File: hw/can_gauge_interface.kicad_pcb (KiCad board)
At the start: 4 copper layers, 75 x 75 mm, 61 parts, among them J1 Conn_02x04_Top_Bottom, J2 Analog, J3 Power debug, J4 Power debug, J5 SPI debug, J6 I^{2}C debug, J7 CAN debug, J8 SWD, U1 STM32C092CBT6, U2 TPS5430DDA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

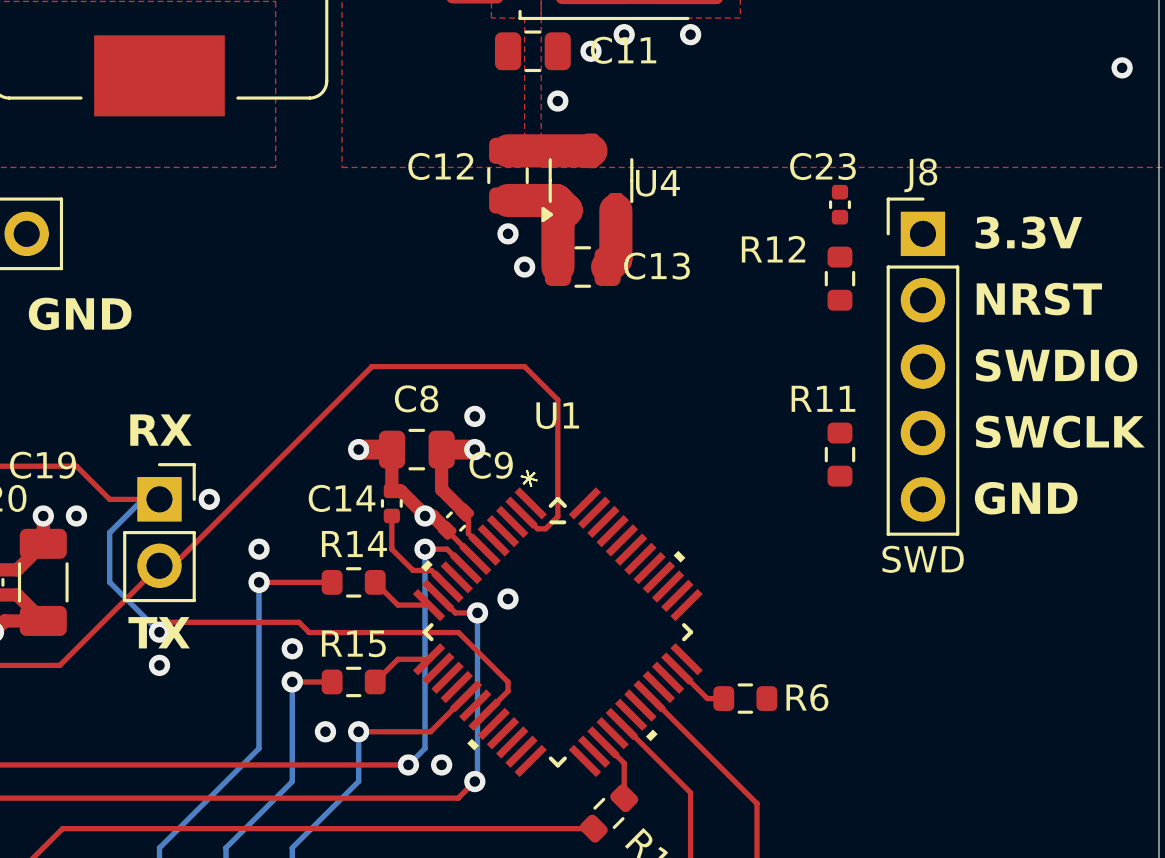
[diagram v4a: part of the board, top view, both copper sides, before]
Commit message: pcb: swd routing
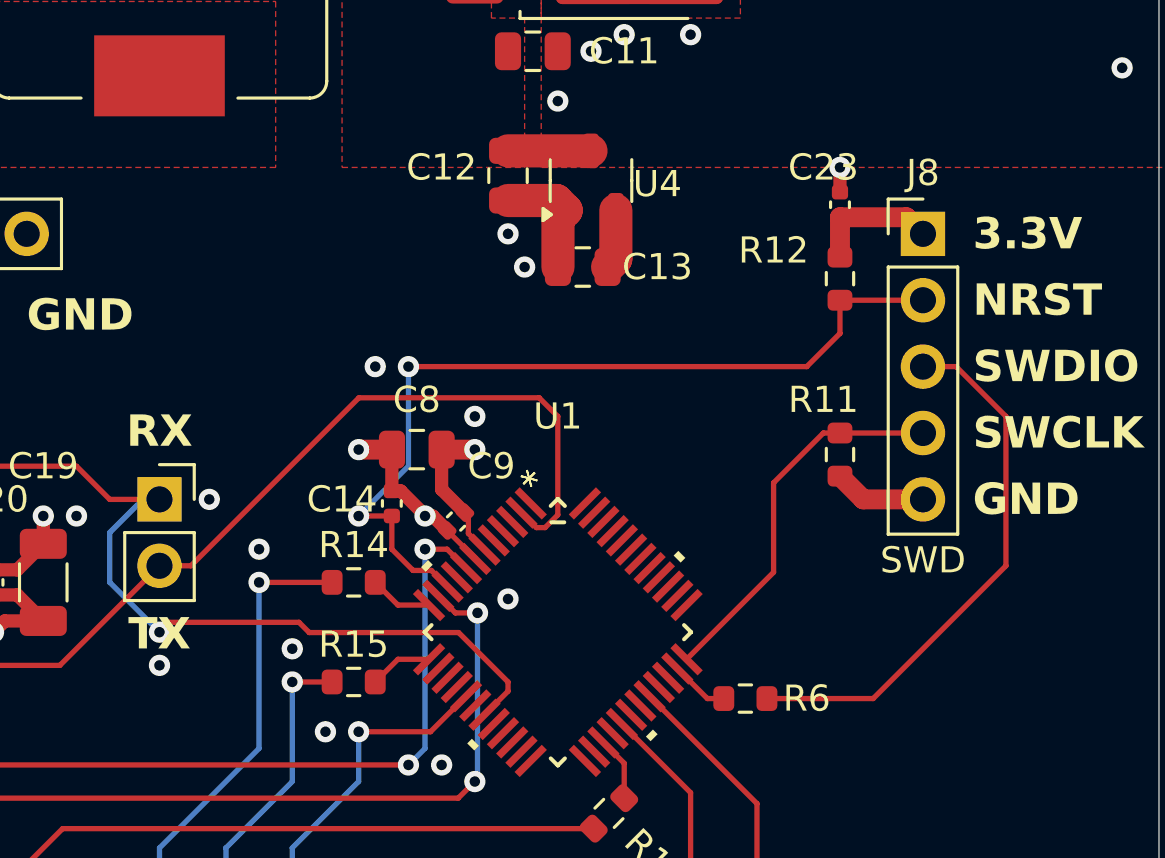
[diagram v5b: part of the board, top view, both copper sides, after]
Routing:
- net NRST: track 3.99 -> 33.2 mm, vias 0 -> 2
- net SWDIO: track 0.00 -> 20.9 mm
- net SWCLK: track 0.00 -> 14.6 mm
- net +3.3V: track 30.5 -> 35.5 mm
- net GND: track 55.6 -> 60.1 mm, vias 51 -> 53
- net CAN_TX: track 35.4 -> 33.9 mm
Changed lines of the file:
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@@
+	)
+	(segment
+		(start 140.97 81.28)
+		(end 138.685 81.28)
+		(width 0.762)
+		(layer "F.Cu")
+		(net 1)
 	)
 	(segment
@@
 	)
 	(segment
+		(start 138.685 81.28)
+		(end 137.795 80.39)
+		(width 0.762)
+		(layer "F.Cu")
+		(net 1)
+	)
+	(segment
 		(start 107.906178 108.541178)
 		(end 107.95 108.585)
@@
 		(start 103.7336 85.09)
 		(end 102.235 85.09)
+		(width 0.508)
+		(layer "F.Cu")
+		(net 1)
+	)
+	(segment
+		(start 137.795 69.525)
+		(end 137.795 68.58)
 		(width 0.508)
 		(layer "F.Cu")
@@
 	)
 	(via
+		(at 137.795 68.58)
+		(size 0.8128)
+		(drill 0.4)
+		(layers "F.Cu" "B.Cu")
+		(free yes)
+		(net 1)
+	)
+	(via
 		(at 132.08 55.245)
 		(size 0.8128)
@@
 	(via
 		(at 123.825 78.105)
+		(size 0.8128)
+		(drill 0.4)
+		(layers "F.Cu" "B.Cu")
+		(free yes)
+		(net 1)
+	)
+	(via
+		(at 120.015 76.2)
 		(size 0.8128)
 		(drill 0.4)
@@
 	)
 	(segment
+		(start 140.335 70.485)
+		(end 140.97 71.12)
+		(width 0.762)
+		(layer "F.Cu")
+		(net 7)
+	)
+	(segment
 		(start 103.505 104.14)
 		(end 103.505 102.235)
@@
 		(end 137.16 102.235)
 		(width 0.508)
+		(layer "F.Cu")
+		(net 7)
+	)
+	(segment
+		(start 137.795 70.485)
+		(end 140.335 70.485)
+		(width 0.762)
 		(layer "F.Cu")
 		(net 7)
@@
 	)
 	(segment
+		(start 137.795 70.485)
+		(end 137.795 72.01)
+		(width 0.762)
+		(layer "F.Cu")
+		(net 7)
+	)
+	(segment
 		(start 131.445 104.775)
 		(end 130.81 104.775)
@@
 	)
 	(segment
+		(start 136.525 76.2)
+		(end 137.795 74.93)
+		(width 0.2032)
+		(layer "F.Cu")
+		(net 9)
+	)
+	(segment
+		(start 120.65 81.915)
+		(end 119.38 81.915)
+		(width 0.2032)
+		(layer "F.Cu")
+		(net 9)
+	)
+	(segment
+		(start 137.795 74.93)
+		(end 137.795 73.66)
+		(width 0.2032)
+		(layer "F.Cu")
+		(net 9)
+	)
+	(segment
 		(start 122.781119 84.615991)
 		(end 122.163236 83.998108)
@@
 	)
 	(segment
+		(start 140.97 73.66)
+		(end 137.795 73.66)
+		(width 0.2032)
+		(layer "F.Cu")
+		(net 9)
+	)
+	(segment
+		(start 121.285 76.2)
+		(end 136.525 76.2)
+		(width 0.2032)
+		(layer "F.Cu")
+		(net 9)
+	)
+	(segment
 		(start 121.463108 83.998108)
 		(end 120.65 83.185)
@@
 		(net 9)
 	)
+	(via
+		(at 121.285 76.2)
+		(size 0.8128)
+		(drill 0.4)
+		(layers "F.Cu" "B.Cu")
+		(net 9)
+	)
+	(via
+		(at 119.38 81.915)
+		(size 0.8128)
+		(drill 0.4)
+		(layers "F.Cu" "B.Cu")
+		(net 9)
+	)
+	(segment
+		(start 119.38 81.915)
+		(end 121.285 80.01)
+		(width 0.2032)
+		(layer "B.Cu")
+		(net 9)
+	)
+	(segment
+		(start 121.285 80.01)
+		(end 121.285 76.2)
+		(width 0.2032)
+		(layer "B.Cu")
+		(net 9)
+	)
 	(segment
 		(start 122.764338 83.185)
@@
 	)
 	(segment
+		(start 126.511839 82.359449)
+		(end 127 81.871288)
+		(width 0.2032)
+		(layer "F.Cu")
+		(net 34)
+	)
+	(segment
+		(start 127 81.871288)
+		(end 127 78.105)
+		(width 0.2032)
+		(layer "F.Cu")
+		(net 34)
+	)
+	(segment
 		(start 111.76 83.82)
 		(end 107.95 87.63)
@@
 	)
 	(segment
-		(start 127 81.936342)
-		(end 127 77.47)
-		(width 0.2032)
-		(layer "F.Cu")
-		(net 34)
-	)
-	(segment
 		(start 107.95 87.63)
 		(end 105.0036 87.63)
@@
 	)
 	(segment
-		(start 127 77.47)
-		(end 125.73 76.2)
+		(start 127 78.105)
+		(end 126.2878 77.3928)
 		(width 0.2032)
 		(layer "F.Cu")
@@
 	)
 	(segment
-		(start 125.73 76.2)
-		(end 119.889099 76.2)
+		(start 112.962081 83.82)
+		(end 111.76 83.82)
 		(width 0.2032)
 		(layer "F.Cu")
@@
 	)
 	(segment
-		(start 126.530893 82.405449)
-		(end 127 81.936342)
+		(start 126.2878 77.3928)
+		(end 119.389281 77.3928)
 		(width 0.2032)
 		(layer "F.Cu")
@@
 	)
 	(segment
+		(start 126.181431 82.359449)
+		(end 126.511839 82.359449)
+		(width 0.2032)
+		(layer "F.Cu")
+		(net 34)
+	)
+	(segment
+		(start 119.389281 77.3928)
+		(end 112.962081 83.82)
+		(width 0.2032)
+		(layer "F.Cu")
+		(net 34)
+	)
+	(segment
 		(start 125.609546 81.787564)
-		(end 126.227431 82.405449)
+		(end 126.181431 82.359449)
 		(width 0.2032)
 		(layer "F.Cu")
@@
 	)
 	(segment
-		(start 112.269099 83.82)
-		(end 111.76 83.82)
-		(width 0.2032)
-		(layer "F.Cu")
-		(net 34)
-	)
-	(segment
-		(start 126.227431 82.405449)
-		(end 126.530893 82.405449)
-		(width 0.2032)
-		(layer "F.Cu")
-		(net 34)
-	)
-	(segment
-		(start 119.889099 76.2)
-		(end 112.269099 83.82)
-		(width 0.2032)
-		(layer "F.Cu")
-		(net 34)
-	)
-	(segment
+		(start 144.145 83.82)
+		(end 144.145 78.105)
+		(width 0.2032)
+		(layer "F.Cu")
+		(net 35)
+	)
+	(segment
+		(start 144.145 78.105)
+		(end 142.24 76.2)
+		(width 0.2032)
+		(layer "F.Cu")
+		(net 35)
+	)
+	(segment
+		(start 142.24 76.2)
+		(end 140.97 76.2)
+		(width 0.2032)
+		(layer "F.Cu")
+		(net 35)
+	)
+	(segment
+		(start 139.065 88.9)
+		(end 144.145 83.82)
+		(width 0.2032)
+		(layer "F.Cu")
+		(net 35)
+	)
+	(segment
+		(start 135 88.9)
+		(end 139.065 88.9)
+		(width 0.2032)
+		(layer "F.Cu")
+		(net 35)
+	)
+	(segment
+		(start 137.795 78.74)
+		(end 140.97 78.74)
+		(width 0.2032)
+		(layer "F.Cu")
+		(net 38)
+	)
+	(segment
+		(start 135.255 84.06789)
+		(end 135.255 80.645)
+		(width 0.2032)
+		(layer "F.Cu")
+		(net 38)
+	)
+	(segment
+		(start 131.925989 87.396901)
+		(end 135.255 84.06789)
+		(width 0.2032)
+		(layer "F.Cu")
+		(net 38)
+	)
+	(segment
+		(start 137.16 78.74)
+		(end 137.795 78.74)
+		(width 0.2032)
+		(layer "F.Cu")
+		(net 38)
+	)
+	(segment
+		(start 135.255 80.645)
+		(end 137.16 78.74)
+		(width 0.2032)
+		(layer "F.Cu")
+		(net 38)
+	)
+	(segment

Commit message: pcb: 3v3 routing
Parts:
- moved R12 3.59 mm to (135.3, 75.4)
- moved R9 1.91 mm to (102.2, 102.2)
- moved C15 1.62 mm to (106.0, 101.9), turned to -90 degrees
- moved C23 1.33 mm to (138.4, 68.8)
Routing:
- net +3.3V: track 35.5 -> 136.2 mm, vias 3 -> 6
- net GND: track 60.1 -> 65.6 mm, vias 53 -> 55
- net DAC_~{CS}: track 34.7 -> 35.5 mm
- net NRST: track 33.2 -> 32.5 mm
- added copper zone on F.Cu, net +3.3V

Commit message: pcb: 5v routing
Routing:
- net +5V: track 8.30 -> 74.9 mm, vias 1 -> 4
- net GND: vias 55 -> 59
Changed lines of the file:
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@@
+	)
+	(via
+		(at 108.585 81.915)
+		(size 0.8128)
+		(drill 0.4)
+		(layers "F.Cu" "B.Cu")
+		(free yes)
+		(net 1)
 	)
 	(via
@@
 	)
 	(via
-		(at 108.585 81.915)
-		(size 0.8128)
-		(drill 0.4)
-		(layers "F.Cu" "B.Cu")
-		(free yes)
-		(net 1)
-	)
-	(via
 		(at 121.92 81.915)
 		(size 0.8128)
@@
 	)
 	(via
+		(at 113.03 109.855)
+		(size 0.8128)
+		(drill 0.4)
+		(layers "F.Cu" "B.Cu")
+		(free yes)
+		(net 1)
+	)
+	(via
 		(at 125.095 85.09)
 		(size 0.8128)
@@
 	)
 	(via
+		(at 119.38 68.58)
+		(size 0.8128)
+		(drill 0.4)
+		(layers "F.Cu" "B.Cu")
+		(free yes)
+		(net 1)
+	)
+	(via
 		(at 148.59 64.77)
 		(size 0.8128)
@@
 	)
 	(via
+		(at 100.329999 73.025)
+		(size 0.8128)
+		(drill 0.4)
+		(layers "F.Cu" "B.Cu")
+		(free yes)
+		(net 1)
+	)
+	(via
 		(at 122.555 91.44)
 		(size 0.8128)
@@
 	(via
 		(at 90.17 60.96)
+		(size 0.8128)
+		(drill 0.4)
+		(layers "F.Cu" "B.Cu")
+		(free yes)
+		(net 1)
+	)
+	(via
+		(at 108.585 78.105)
 		(size 0.8128)
 		(drill 0.4)
@@
 	)
 	(segment
+		(start 111.125 110.49)
+		(end 111.76 109.855)
+		(width 0.762)
+		(layer "F.Cu")
+		(net 5)
+	)
+	(segment
 		(start 105.41 83.975)
 		(end 103.8886 83.975)
@@
 	)
 	(segment
-		(start 107.315 82.98)
-		(end 107.315 81.915)
-		(width 0.508)
+		(start 101.599999 71.12)
+		(end 101.6 72.39)
+		(width 1.27)
 		(layer "F.Cu")
 		(net 5)
@@
 	)
 	(segment
+		(start 101.6 72.39)
+		(end 107.315 78.105)
+		(width 1.27)
+		(layer "F.Cu")
+		(net 5)
+	)
+	(segment
 		(start 106.32 83.975)
 		(end 107.315 82.98)
@@
 	)
 	(segment
+		(start 111.125 111.76)
+		(end 111.125 110.49)
+		(width 0.762)
+		(layer "F.Cu")
+		(net 5)
+	)
+	(segment
 		(start 105.41 83.975)
 		(end 106.32 83.975)
@@
 	)
 	(segment
+		(start 107.315 81.915)
+		(end 107.315 82.98)
+		(width 1.27)
+		(layer "F.Cu")
+		(net 5)
+	)
+	(segment
 		(start 103.8886 83.975)
 		(end 103.7336 83.82)
@@
 	(via
 		(at 107.315 81.915)
-		(size 0.8128)
-		(drill 0.4)
-		(layers "F.Cu" "B.Cu")
-		(net 5)
-	)
+		(size 1.2192)
+		(drill 0.7)
+		(layers "F.Cu" "B.Cu")
+		(net 5)
+	)
+	(via
+		(at 120.015 67.31)
+		(size 1.2192)
+		(drill 0.7)
+		(layers "F.Cu" "B.Cu")
+		(free yes)
+		(net 5)
+	)
+	(via
+		(at 107.315 78.105)
+		(size 1.2192)
+		(drill 0.7)
+		(layers "F.Cu" "B.Cu")
+		(net 5)
+	)
+	(via
+		(at 111.76 109.855)
+		(size 1.2192)
+		(drill 0.7)
+		(layers "F.Cu" "B.Cu")
+		(net 5)
+	)
+	(segment
+		(start 107.95 88.9)
+		(end 107.95 106.045)
+		(width 1.27)
+		(layer "B.Cu")
+		(net 5)
+	)
+	(segment
+		(start 120.015 67.31)
+		(end 102.87 67.31)
+		(width 1.27)
+		(layer "B.Cu")
+		(net 5)
+	)
+	(segment
+		(start 107.315 78.105)
+		(end 107.315 81.915)
+		(width 1.27)
+		(layer "B.Cu")
+		(net 5)
+	)
+	(segment
+		(start 101.599999 68.580001)
+		(end 101.599999 71.12)
+		(width 1.27)
+		(layer "B.Cu")
+		(net 5)
+	)
+	(segment
+		(start 107.95 106.045)
+		(end 111.76 109.855)
+		(width 1.27)
+		(layer "B.Cu")
+		(net 5)
+	)
+	(segment
+		(start 102.87 67.31)
+		(end 101.599999 68.580001)
+		(width 1.27)
+		(layer "B.Cu")
+		(net 5)
+	)
+	(segment
+		(start 107.315 88.265)
+		(end 107.95 88.9)
+		(width 1.27)
+		(layer "B.Cu")
+		(net 5)
+	)
+	(segment
+		(start 107.315 81.915)
+		(end 107.315 88.265)
+		(width 1.27)
+		(layer "B.Cu")
+		(net 5)
+	)

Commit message: pcb: drc
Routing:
- net GND: track 65.6 -> 69.3 mm, vias 59 -> 64
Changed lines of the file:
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@@
 			)
 		)
-		(pad "" smd roundrect
-			(at -0.5 -0.5 315)
-			(size 0.806226 0.806226)
-			(layers "F.Paste")
-			(roundrect_rratio 0.25)
-		)
-		(pad "" smd roundrect
-			(at -0.5 0.5 315)
-			(size 0.806226 0.806226)
-			(layers "F.Paste")
-			(roundrect_rratio 0.25)
-		)
 		(pad "" smd custom
 			(at -0.499999 -1.2875 315)
@@
 			)
 		)
-		(pad "" smd roundrect
-			(at 0.5 -0.5 315)
-			(size 0.806226 0.806226)
-			(layers "F.Paste")
-			(roundrect_rratio 0.25)
-		)
-		(pad "" smd roundrect
-			(at 0.5 0.5 315)
-			(size 0.806226 0.806226)
-			(layers "F.Paste")
-			(roundrect_rratio 0.25)
-		)
 		(pad "" smd custom
 			(at 1.2875 -1.2875 315)
@@
 			(pintype "power_in")
 		)
-		(pad "21" thru_hole circle
-			(at -1 -1 315)
-			(size 0.5 0.5)
-			(drill 0.2)
-			(property pad_prop_heatsink)
-			(layers "*.Cu")
-			(remove_unused_layers no)
-			(net 1 "GND")
-			(pinfunction "EP")
-			(pintype "passive")
-		)
-		(pad "21" thru_hole circle
-			(at -1 0 315)
-			(size 0.5 0.5)
-			(drill 0.2)
-			(property pad_prop_heatsink)
-			(layers "*.Cu")
-			(remove_unused_layers no)
-			(net 1 "GND")
-			(pinfunction "EP")
-			(pintype "passive")
-		)
-		(pad "21" thru_hole circle
-			(at -1 1 315)
-			(size 0.5 0.5)
-			(drill 0.2)
-			(property pad_prop_heatsink)
-			(layers "*.Cu")
-			(remove_unused_layers no)
-			(net 1 "GND")
-			(pinfunction "EP")
-			(pintype "passive")
-		)
-		(pad "21" thru_hole circle
-			(at 0 -1 315)
-			(size 0.5 0.5)
-			(drill 0.2)
-			(property pad_prop_heatsink)
-			(layers "*.Cu")
-			(remove_unused_layers no)
-			(net 1 "GND")
-			(pinfunction "EP")
-			(pintype "passive")
-		)
-		(pad "21" thru_hole circle
-			(at 0 0 315)
-			(size 0.5 0.5)
-			(drill 0.2)
-			(property pad_prop_heatsink)
-			(layers "*.Cu")
-			(remove_unused_layers no)
-			(net 1 "GND")
-			(pinfunction "EP")
-			(pintype "passive")
-		)
-		(pad "21" smd rect
-			(at 0 0 315)
-			(size 2.5 2.5)
-			(property pad_prop_heatsink)
-			(layers "B.Cu")
-			(net 1 "GND")
-			(pinfunction "EP")
-			(pintype "passive")
-			(zone_connect 2)
-		)
 		(pad "21" smd rect
 			(at 0 0 315)
@@
 			(zone_connect 2)
 		)
-		(pad "21" thru_hole circle
-			(at 0 1 315)
-			(size 0.5 0.5)
-			(drill 0.2)
-			(property pad_prop_heatsink)
-			(layers "*.Cu")
-			(remove_unused_layers no)
-			(net 1 "GND")
-			(pinfunction "EP")
-			(pintype "passive")
-		)
-		(pad "21" thru_hole circle
-			(at 1 -1 315)
-			(size 0.5 0.5)
-			(drill 0.2)
-			(property pad_prop_heatsink)
-			(layers "*.Cu")
-			(remove_unused_layers no)
-			(net 1 "GND")
-			(pinfunction "EP")
-			(pintype "passive")
-		)
-		(pad "21" thru_hole circle
-			(at 1 0 315)
-			(size 0.5 0.5)
-			(drill 0.2)
-			(property pad_prop_heatsink)
-			(layers "*.Cu")
-			(remove_unused_layers no)
-			(net 1 "GND")
-			(pinfunction "EP")
-			(pintype "passive")
-		)
-		(pad "21" thru_hole circle
-			(at 1 1 315)
-			(size 0.5 0.5)
-			(drill 0.2)
-			(property pad_prop_heatsink)
-			(layers "*.Cu")
-			(remove_unused_layers no)
-			(net 1 "GND")
-			(pinfunction "EP")
-			(pintype "passive")
-		)
 		(embedded_fonts no)
 		(model "${KICAD9_3DMODEL_DIR}/Package_DFN_QFN.3dshapes/Texas_RGW0020A_VQFN-20-1EP_5x5mm_P0.65mm_EP3.15x3.15mm.wrl"
@@
 		(sheetname "/")
 		(sheetfile "can_gauge_interface.kicad_sch")
+		(clearance 0.199898)
 		(attr smd)
 		(fp_line
@@
 	)
 	(segment
+		(start 103.90554 106.27946)
+		(end 102.235 107.95)
+		(width 0.3048)
+		(layer "F.Cu")
+		(net 1)
+	)
+	(segment
 		(start 123.841778 83.543422)
 		(end 122.765178 82.466822)
@@
 	)
 	(segment
+		(start 127.005002 72.39)
+		(end 125.73 72.39)
+		(width 1.27)
+		(layer "F.Cu")
+		(net 1)
+	)
+	(segment
 		(start 104.775 104.227644)
 		(end 104.775 102.87)
@@
 	)
 	(segment
+		(start 102.585761 106.68)
+		(end 102.235 106.68)
+		(width 0.3048)
+		(layer "F.Cu")
+		(net 1)
+	)
+	(segment
 		(start 104.183822 104.818822)
 		(end 104.775 104.227644)
@@
 	)
 	(segment
-		(start 102.729975 106.535786)
-		(end 102.235 106.535786)
-		(width 0.3048)
-		(layer "F.Cu")
-		(net 1)
-	)
-	(segment
 		(start 130.2823 107.2077)
 		(end 130.175 107.315)
@@
 	)
 	(segment
-		(start 103.90554 106.27946)
-		(end 102.942107 107.242893)
-		(width 0.3048)
-		(layer "F.Cu")
-		(net 1)
-	)
-	(segment
 		(start 105.41 84.935)
 		(end 106.32 84.935)
@@
 	(segment
 		(start 100.104841 109.16092)
-		(end 100.820786 108.444975)
+		(end 100.965 108.300761)
 		(width 0.3048)
 		(layer "F.Cu")
@@
 	)
 	(segment
+		(start 103.44592 105.819841)
+		(end 102.585761 106.68)
+		(width 0.3048)
+		(layer "F.Cu")
+		(net 1)
+	)
+	(segment
 		(start 120.65 80.955)
 		(end 120.98676 80.955)
@@
 	)
 	(segment
+		(start 125.095 69.844998)
+		(end 125.095 71.12)
+		(width 1.27)
+		(layer "F.Cu")
+		(net 1)
+	)
+	(segment
 		(start 91.44 59.69)
 		(end 92.71 59.69)
@@
 	)
 	(segment
-		(start 100.820786 108.444975)
-		(end 100.820786 107.95)
+		(start 100.965 108.300761)
+		(end 100.965 107.95)
 		(width 0.3048)
 		(layer "F.Cu")
@@
 	)
 	(segment
-		(start 103.44592 105.819841)
-		(end 102.729975 106.535786)
-		(width 0.3048)
-		(layer "F.Cu")
-		(net 1)
-	)
-	(segment
 		(start 127.005002 72.39)
 		(end 127.005002 70.534999)
@@
 	)
 	(via
+		(at 102.235 106.68)
+		(size 0.8128)
+		(drill 0.4)
+		(layers "F.Cu" "B.Cu")
+		(net 1)
+	)
+	(via
 		(at 129.54 63.5)
 		(size 0.8128)
@@
 	)
 	(via
+		(at 103.505 107.95)
+		(size 0.8128)
+		(drill 0.4)
+		(layers "F.Cu" "B.Cu")
+		(net 1)
+	)
+	(via
 		(at 120.015 76.2)
 		(size 0.8128)
@@
 	)
 	(via
-		(at 113.03 104.775)
+		(at 114.3 105.41)
 		(size 0.8128)
 		(drill 0.4)
@@
 	)
 	(via
+		(at 113.03 105.41)
+		(size 0.8128)
+		(drill 0.4)
+		(layers "F.Cu" "B.Cu")
+		(free yes)
+		(net 1)
+	)
+	(via
 		(at 113.03 109.855)
 		(size 0.8128)
@@
 	)
 	(via
+		(at 100.965 107.95)
+		(size 0.8128)
+		(drill 0.4)
+		(layers "F.Cu" "B.Cu")
+		(net 1)
+	)
+	(via
 		(at 104.775 102.87)
 		(size 0.8128)
@@
 		(net 1)
 	)
+	(via
+		(at 102.235 109.22)
+		(size 0.8128)
+		(drill 0.4)
+		(layers "F.Cu" "B.Cu")
+		(net 1)
+	)
